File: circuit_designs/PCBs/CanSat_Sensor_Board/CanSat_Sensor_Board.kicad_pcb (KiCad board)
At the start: 4 copper layers, 95 x 95 mm, 46 parts, among them J1 Power Board, J10 CPL 2, J11 CPL 3, J2 Camera Board, J3 Hall Effect, J4 GPS, J5 LED, J6 Fin 1, J7 Fin 2, J8 Camera, J9 CPL 1, Y1 32.768kHz

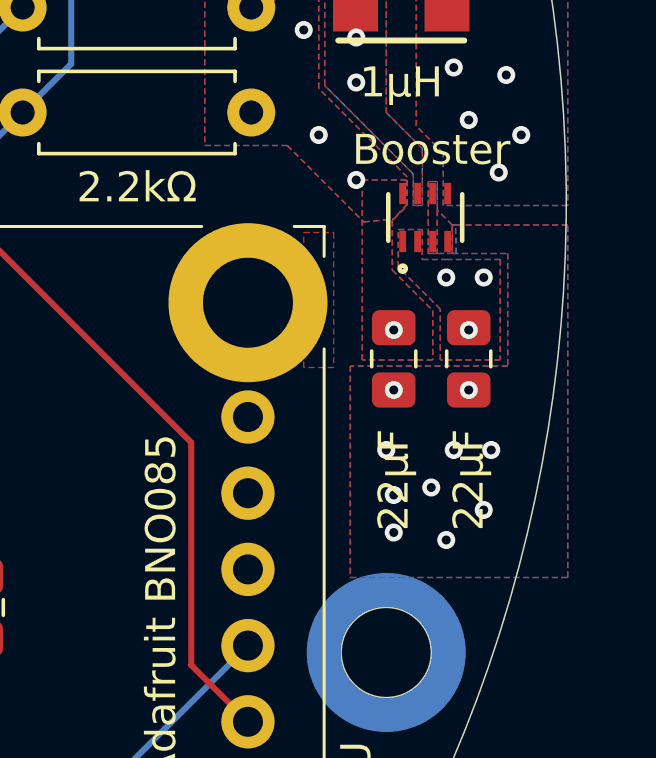
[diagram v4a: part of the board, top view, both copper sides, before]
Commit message: fixed errors and exposed copper for thermal pads
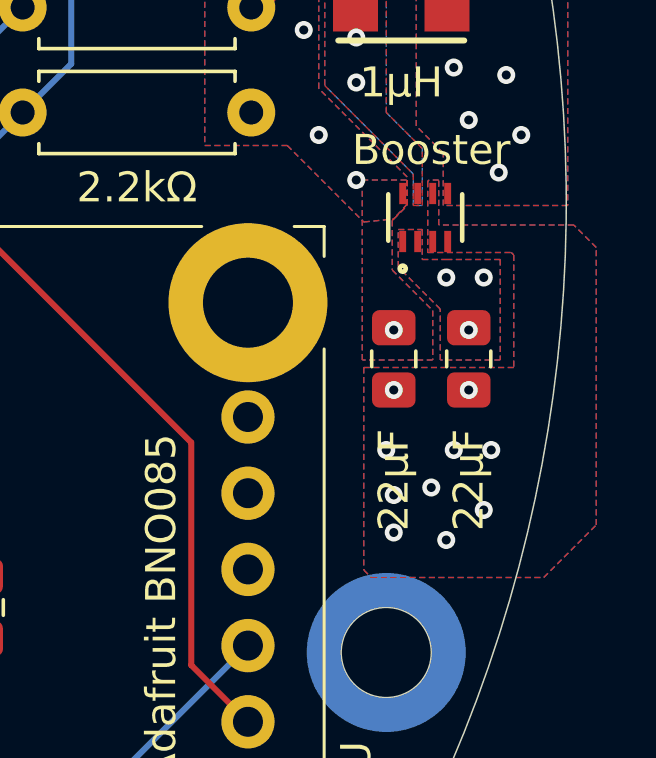
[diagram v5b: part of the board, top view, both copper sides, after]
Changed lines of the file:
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@@
-	)
-	(zone
-		(net 20)
-		(net_name "GND")
-		(layer "F.Cu")
-		(hatch edge 0.5)
-		(priority 3)
-		(connect_pads yes
-			(clearance 0.1)
-		)
-		(min_thickness 0.25)
-		(filled_areas_thickness no)
-		(fill yes
-			(thermal_gap 0.5)
-			(thermal_bridge_width 0.5)
-		)
-		(polygon
-			(pts
-				(xy 193.2 101.7) (xy 193.7 101.7) (xy 193.7 100.75) (xy 193.2 100.25)
-			)
-		)
 	)
 	(zone
@@
 	)
 	(zone
-		(net 20)
-		(net_name "GND")
-		(layer "F.Cu")
-		(hatch edge 0.5)
-		(priority 13)
-		(connect_pads
-			(clearance 0)
-		)
-		(min_thickness 0.25)
-		(filled_areas_thickness no)
-		(fill yes
-			(thermal_gap 0.5)
-			(thermal_bridge_width 0.5)
-		)
-		(polygon
-			(pts
-				(xy 188.75 105.5) (xy 188.75 101) (xy 189.75 101) (xy 189.75 105.5)
-			)
-		)
-	)
-	(zone
 		(net 45)
 		(net_name "/7.4V")
@@
 		(net 20)
 		(net_name "GND")
-		(layer "F.Cu")
-		(hatch edge 0.5)
-		(priority 2)
-		(connect_pads yes
-			(clearance 0.1)
-		)
-		(min_thickness 0.25)
-		(filled_areas_thickness no)
-		(fill yes
-			(thermal_gap 0.5)
-			(thermal_bridge_width 0.5)
-		)
-		(polygon
-			(pts
-				(xy 192.9 99.3) (xy 193.2 99.3) (xy 193.2 101.7) (xy 192.9 101.7)
-			)
-		)
-	)
-	(zone
-		(net 20)
-		(net_name "GND")
 		(layers "F&B.Cu")
 		(hatch edge 0.5)
 		(priority 4)
 		(connect_pads yes
-			(clearance 0)
-		)
-		(min_thickness 0.25)
-		(filled_areas_thickness no)
-		(fill yes
-			(thermal_gap 0.5)
-			(thermal_bridge_width 0.5)
-		)
-		(polygon
-			(pts
-				(xy 193.7 101.7) (xy 195.55 101.7) (xy 195.55 105.45) (xy 190.3 105.45) (xy 190.3 112.5) (xy 197.55 112.5)
-				(xy 197.55 100.75) (xy 193.7 100.75)
+			(clearance 0.1)
+		)
+		(min_thickness 0.25)
+		(filled_areas_thickness no)
+		(fill yes
+			(thermal_gap 0.5)
+			(thermal_bridge_width 0.5)
+		)
+		(polygon
+			(pts
+				(xy 195.75 105.5) (xy 190.75 105.5) (xy 190.75 112.25) (xy 191 112.5) (xy 196.75 112.5) (xy 198.5 110.75)
+				(xy 198.5 101.5) (xy 197.75 100.75) (xy 193.25 100.75) (xy 193.25 99.25) (xy 192.923538 99.25) (xy 192.881553 99.291985)
+				(xy 192.881553 101.667191) (xy 195.667191 101.667191) (xy 195.75 101.75)
 			)
 		)
@@
 	)
 	(zone
-		(net 20)
-		(net_name "GND")
-		(layer "B.Cu")
-		(hatch edge 0.5)
-		(priority 8)
-		(connect_pads yes
-			(clearance 0.1)
-		)
-		(min_thickness 0.25)
-		(filled_areas_thickness no)
-		(fill yes
-			(thermal_gap 0.5)
-			(thermal_bridge_width 0.5)
-		)
-		(polygon
-			(pts
-				(xy 193.7 100.75) (xy 193.2 100.25) (xy 193.2 99.3) (xy 192.9 99.3) (xy 192.9 101.7) (xy 193.825449 101.693865)
-				(xy 193.8201 100.747018)
-			)
-		)
-	)
-	(zone
 		(net 69)
 		(net_name "/SW")
@@
 			)
 		)
+	)
+	(zone
+		(net 0)
+		(net_name "")
+		(layer "B.Mask")
+		(hatch edge 0.5)
+		(priority 4)
+		(connect_pads yes
+			(clearance 0.1)
+		)
+		(min_thickness 0.25)
+		(filled_areas_thickness no)
+		(fill yes
+			(thermal_gap 0.5)
+			(thermal_bridge_width 0.5)
+		)
+		(polygon
+			(pts
+				(xy 190.75 112.5) (xy 195.575573 112.5) (xy 195.575573 112.5) (xy 195.575573 90.687799) (xy 195.575573 90.687799)
+				(xy 189.450239 90.687799) (xy 189.450239 99.618367) (xy 190.75 100.918128)
+			)
+		)
